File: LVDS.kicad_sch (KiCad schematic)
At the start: 21 parts, among them J13 DF13C-3P-1.25V_21_, J14 PinHeader_1x2_P2.54mm_Drill1.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, J15 PinHeader_1x2_P2.54mm_Drill1.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, J16 QSH-030-01-X-D-A-XX, J3 QSH-030-01-X-D-A-XX, U10 TCAN1042HVDQ1, U11 SN74AVC2T245_UQFN

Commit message: Added second CAN interface, but haven't routed yet
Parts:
- added C175, C176, C177, C178, C179, C180, C181: C_100n_0402, kria-k26-devboard-footprints:C_0402_1005Metric, symbol kria-k26-devboard:C_100n_0402
- added D9: NUP2105LT1G, kria-k26-devboard-footprints:SOT95P237X111-3N, symbol kria-k26-devboard:NUP2105LT1G
- added J17, J18: PinHeader_1x2_P2.54mm_Drill1.02mm, kria-k26-devboard-footprints:PinHeader_1x2_P2.54mm_Drill1.02mm, symbol kria-k26-devboard:PinHeader_1x2_P2.54mm_Drill1.02mm
- added J19: DF13C-3P-1.25V_21_, kria-k26-devboard-footprints:HRS_DF13C-3P-1.25V_21_, symbol kria-k26-devboard:DF13C-3P-1.25V_21_
- added R29, R30: R_60R4_0402, kria-k26-devboard-footprints:R_0402_1005Metric, symbol kria-k26-devboard:R_60R4_0402
- added U56: SN74AVC2T245_UQFN, kria-k26-devboard-footprints:UQFN-10_1.4x1.8x0.5mm_P0.4mm, symbol kria-k26-devboard:SN74AVC2T245_UQFN
- added U62: TCAN1042HVDQ1, kria-k26-devboard-footprints:D0008A_L, symbol kria-k26-devboard:TCAN1042HVDQ1
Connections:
- net GND: now also C175.2, C176.1, C177.1, C178.2, C179.2, C180.2, C181.2, D9.3, J19.2, U56.1 (DIR_{2}), U56.2 (~{OE}), U56.3 (GND), U62.2 (GND), U62.8 (STB)
- net PS_1V8: now also C178.1, U56.10 (DIR_{1}), U56.7 (V_{CCA})
- net PS_3V3: now also C179.1, C180.1, U56.6 (V_{CCB}), U62.5 (VIO)
- net SOM_5V0: now also C181.1, U62.3 (VCC)
- new net: J17.2, R29.2
- new net: U56.4 (B_{2}), U62.4 (RXD)
- new net: U56.5 (B_{1}), U62.1 (TXD)
- new net: J18.2, R30.1
- new net: C175.1, R29.1, R30.2
- new net CAN2_H: C176.2, D9.2, J17.1, J19.3, U62.7 (CANH)
- new net CAN2_L: C177.2, D9.1, J18.1, J19.1, U62.6 (CANL)
- new net HDC22: U56.8 (A_{1})
- new net HDC23: U56.9 (A_{2})
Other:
- moved on the sheet: C29

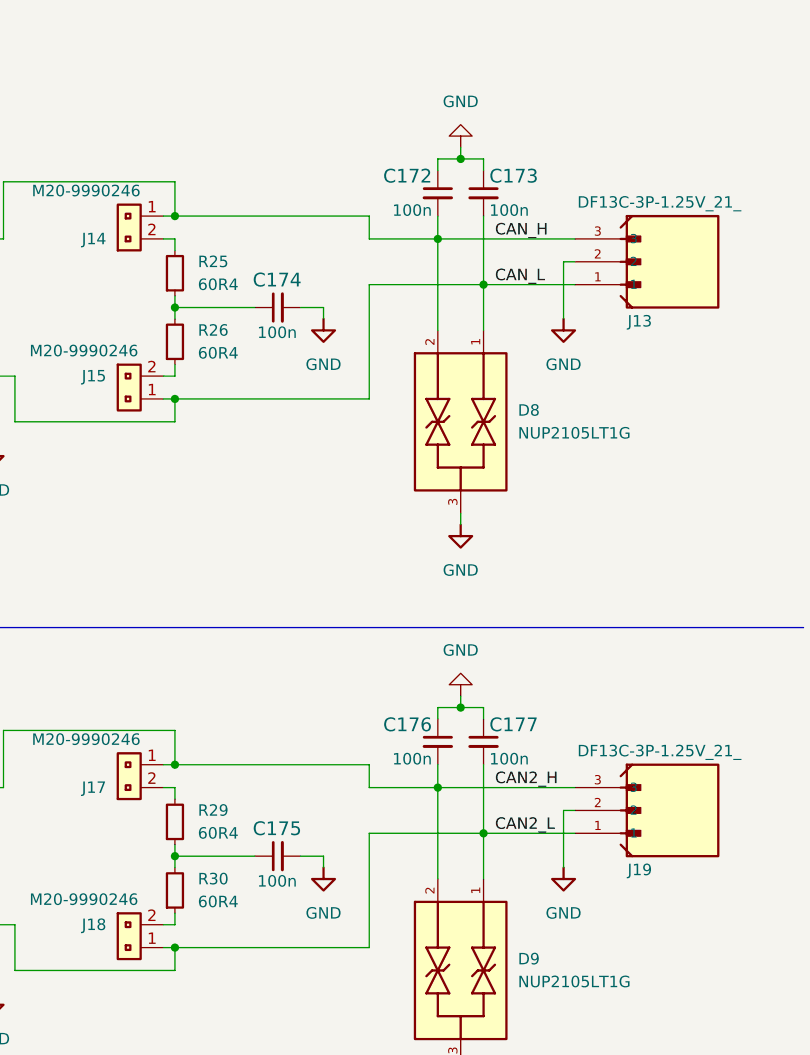
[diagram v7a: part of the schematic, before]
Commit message: Fixed CAN bus filtering/terminating capacitance values
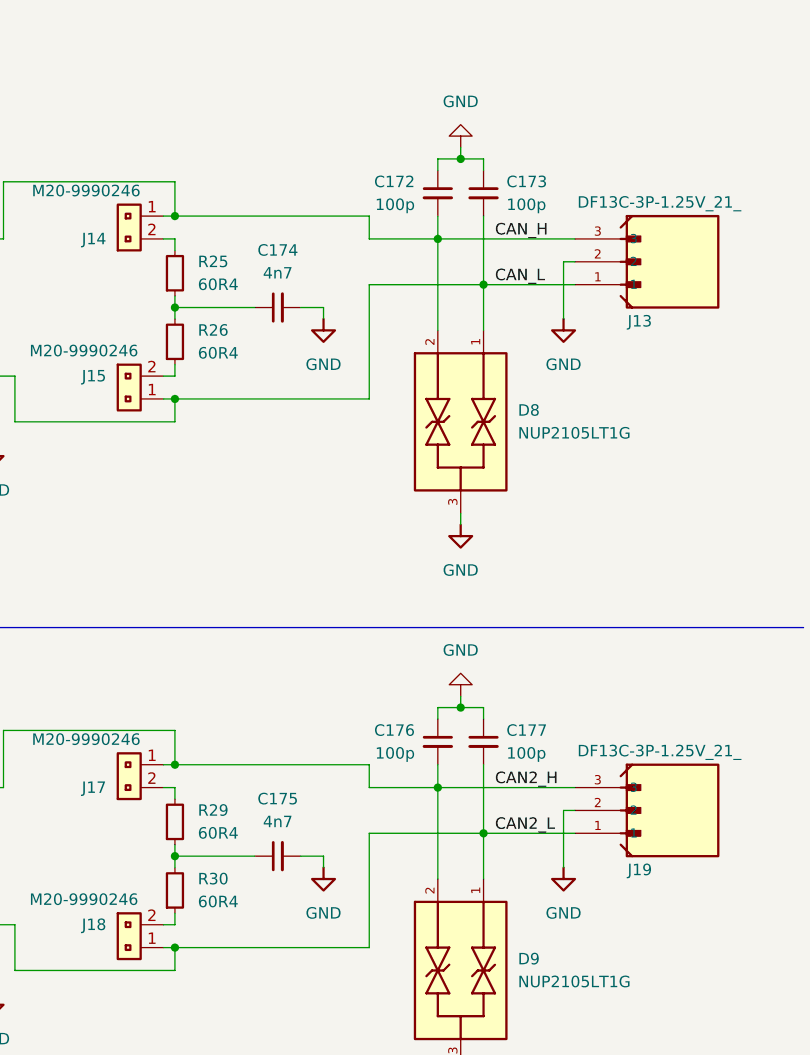
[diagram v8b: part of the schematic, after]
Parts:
- removed C172, C173, C174, C175, C176, C177: C_100n_0402, kria-k26-devboard-footprints:C_0402_1005Metric, symbol kria-k26-devboard:C_100n_0402
- added C172, C173, C176, C177: C_100p_0402, kria-k26-devboard-footprints:C_0402_1005Metric, symbol kria-k26-devboard:C_100p_0402
- added C174, C175: C_4n7_0402, kria-k26-devboard-footprints:C_0402_1005Metric, symbol kria-k26-devboard:C_4n7_0402
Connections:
- net CAN2_H: now also C176.2
- net CAN2_L: now also C177.2
- net CAN_H: now also C172.2
- net CAN_L: now also C173.2
- net GND: now also C172.1, C173.1, C174.2, C175.2, C176.1, C177.1
- net at R29.1, R30.2: now also C175.1
- net at R25.1, R26.2: now also C174.1
